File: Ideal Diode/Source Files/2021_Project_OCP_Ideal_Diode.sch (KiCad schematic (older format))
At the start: 21 parts, among them P101 SMD_1POS_8MM, P102 SMD_1POS_8MM, P103 SMD_1POS_8MM, P104 SMD_1POS_8MM, P105 MH_1POS_2.5MM, P106 MH_1POS_2.5MM, P107 MH_1POS_2.5MM, P108 MH_1POS_2.5MM, Q101 PSMNR70-40SSHJ, U101 ZXTR2112F-7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

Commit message: Add files via upload
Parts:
- removed R101: RC0603FR-07100RL, Passives:R_0603_Handsolder, symbol Resistors_0603:RC0603FR-07100RL
- removed R104: ERA-3AEB103V, Passives:R_0603_Handsolder, symbol Resistors_0603:ERA-3AEB103V
- removed R105: RMCF0603ZT0R00, Passives:R_0603_Handsolder, symbol Resistors_0603:RMCF0603ZT0R00
- added R101: RC0603FR-0716RL, Passives:R_0603_Handsolder, symbol Resistors_0603:RC0603FR-0716RL
- added R104, R105: RC0603FR-07470RL, Passives:R_0603_Handsolder, symbol Resistors_0603:RC0603FR-07470RL
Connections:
- net CATHODE: now also R105.2
- net GND: now also R104.2
- net at U102.1 (OUT): now also R101.1
- net at Q101.1 (G): now also R101.2
- net at U102.3 (IN+): now also R104.1
- net at U102.4 (IN-): now also R105.1
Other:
- note added: "1. REPLACED R104, R105 WITH 16R RESISTOR"
- note added: "20210308_PROJECTS_IdealDiode_A3_00004"
- note added: "A3"
- moved on the sheet: P101, P103
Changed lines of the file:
@@
 Text Notes 8825 825  0    50   ~ 0
 20210120_PROJECTS_IdealDiode_A0_00001
-$Comp
-L Resistors_0603:RC0603FR-07100RL R101
-U 1 1 5FCA2DDC
-P 5825 4950
-F 0 "R101" V 5825 4950 50  0000 C CNN
-F 1 "RC0603FR-07100RL" V 5925 4950 50  0001 C CNN
-F 2 "Passives:R_0603_Handsolder" V 5755 4950 50  0001 C CNN
-F 3 "" V 5905 4950 50  0000 C CNN
-F 4 "Susumu" V 6005 5050 60  0001 C CNN "Manufacturer"
-F 5 "100R" H 5875 5000 50  0000 L CNN "P_Value"
-F 6 "1/10W" V 6125 5250 60  0001 C CNN "P_Rating_U"
-F 7 "1%" H 5900 4875 25  0000 L CNN "P_Tolerance"
-F 8 "0603" H 5900 4925 25  0000 L CNN "Package"
-	1    5825 4950
-	1    0    0    -1
-$EndComp
 Wire Wire Line
 	5825 5100 5825 5150
@@
 Connection ~ 6375 5350
 Wire Wire Line
-	4800 2375 5775 2375
+	4800 2925 5775 2925
 Wire Wire Line
 	4775 5350 5350 5350
@@
 L power:VBUS #PWR0106
 U 1 1 5FCBCFE3
-P 5775 2325
-F 0 "#PWR0106" H 5775 2175 50  0001 C CNN
-F 1 "VBUS" H 5775 2475 50  0000 C CNN
-F 2 "" H 5775 2325 50  0001 C CNN
-F 3 "" H 5775 2325 50  0001 C CNN
-	1    5775 2325
-	1    0    0    -1
-$EndComp
-Wire Wire Line
-	5775 2325 5775 2375
-Connection ~ 5775 2375
-Wire Wire Line
-	5775 2375 6425 2375
+P 5775 2875
+F 0 "#PWR0106" H 5775 2725 50  0001 C CNN
+F 1 "VBUS" H 5775 3025 50  0000 C CNN
+F 2 "" H 5775 2875 50  0001 C CNN
+F 3 "" H 5775 2875 50  0001 C CNN
+	1    5775 2875
+	1    0    0    -1
+$EndComp
+Wire Wire Line
+	5775 2875 5775 2925
+Connection ~ 5775 2925
+Wire Wire Line
+	5775 2925 6425 2925
 $Comp
 L power:GND #PWR0110
@@
 Text Notes 7150 1300 0    47   ~ 0
 1. ADDED DESD34VS2SO (D101)\n2. ADDED 10K (R104)\n3. REPLACED Q101 WITH PSMNR70-40SSHJ\n4. ADDED R105 0R\n5. ADDED R106 ThermaLink
-$Comp
-L Resistors_0603:ERA-3AEB103V R104
-U 1 1 601B6BEA
-P 6375 4400
-F 0 "R104" V 6375 4400 50  0000 C CNN
-F 1 "ERA-3AEB103V" V 6475 4400 50  0001 C CNN
-F 2 "Passives:R_0603_Handsolder" V 6305 4400 50  0001 C CNN
-F 3 "" V 6455 4400 50  0000 C CNN
-F 4 "Panasonic Electronic Components" V 6555 4500 60  0001 C CNN "Manufacturer"
-F 5 "10k" H 6425 4450 50  0000 L CNN "P_Value"
-F 6 "1/10W" V 6675 4700 60  0001 C CNN "P_Rating_U"
-F 7 "0.1%" H 6500 4325 25  0000 C CNN "P_Tolerance"
-F 8 "0603" H 6450 4375 25  0000 L CNN "Package"
-F 9 "P10KDBCT-ND" H 6375 4400 25  0001 C CNN "P_Digikey"
-	1    6375 4400
-	1    0    0    -1
-$EndComp
 Wire Wire Line
 	6375 4250 6375 4025
@@
 	0    -1   1    0
 $EndComp
-$Comp
-L Resistors_0603:RMCF0603ZT0R00 R105
-U 1 1 601B32BA
-P 5350 4400
-F 0 "R105" V 5350 4400 50  0000 C CNN
-F 1 "RMCF0603ZT0R00" V 5450 4400 50  0001 C CNN
-F 2 "Passives:R_0603_Handsolder" V 5280 4400 50  0001 C CNN
-F 3 "" V 5430 4400 50  0000 C CNN
-F 4 "Stackpole Electronics Inc." V 5530 4500 60  0001 C CNN "Manufacturer"
-F 5 "0R" H 5400 4450 50  0000 L CNN "P_Value"
-F 6 "1/10W" V 5650 4700 50  0001 C CNN "P_Rating"
-F 7 "0603" H 5425 4375 25  0000 L CNN "Package"
-	1    5350 4400
-	1    0    0    -1
-$EndComp
 Wire Wire Line
 	5350 4250 5350 4025
@@
 L Connectors:SMD_1POS_8MM P103
 U 1 1 601CC9B9
-P 6575 2375
-F 0 "P103" H 6375 2375 60  0000 C CNN
-F 1 "SMD_1POS_8MM" H 6525 1975 50  0001 C CNN
-F 2 "Connectors_sg:SMD_1POS_8MM" V 7175 2175 60  0001 C CNN
-F 3 "" H 6575 2525 60  0001 C CNN
-F 4 "CUSTOM" H 7125 3025 50  0001 C CNN "Manufacturer"
-F 5 "1POS" H 6633 2508 50  0001 C CNN "P_Value"
-F 6 "##" H 7125 2825 60  0001 C CNN "P_Rating_U"
-F 7 "8MM" H 7125 2925 60  0001 C CNN "P_Tolerance"
-F 8 "SMD" H 7125 3125 60  0001 C CNN "Package"
-	1    6575 2375
+P 6575 2925
+F 0 "P103" H 6375 2925 60  0000 C CNN
+F 1 "SMD_1POS_8MM" H 6525 2525 50  0001 C CNN
+F 2 "Connectors_sg:SMD_1POS_8MM" V 7175 2725 60  0001 C CNN
+F 3 "" H 6575 3075 60  0001 C CNN
+F 4 "CUSTOM" H 7125 3575 50  0001 C CNN "Manufacturer"
+F 5 "1POS" H 6633 3058 50  0001 C CNN "P_Value"
+F 6 "##" H 7125 3375 60  0001 C CNN "P_Rating_U"
+F 7 "8MM" H 7125 3475 60  0001 C CNN "P_Tolerance"
+F 8 "SMD" H 7125 3675 60  0001 C CNN "Package"
+	1    6575 2925
 	-1   0    0    1
 $EndComp
@@
 L Connectors:SMD_1POS_8MM P101
 U 1 1 601CD7CA
-P 4650 2375
-F 0 "P101" H 4450 2375 60  0000 C CNN
-F 1 "SMD_1POS_8MM" H 4600 1975 50  0001 C CNN
-F 2 "Connectors_sg:SMD_1POS_8MM" V 5250 2175 60  0001 C CNN
-F 3 "" H 4650 2525 60  0001 C CNN
-F 4 "CUSTOM" H 5200 3025 50  0001 C CNN "Manufacturer"
-F 5 "1POS" H 4708 2508 50  0001 C CNN "P_Value"
-F 6 "##" H 5200 2825 60  0001 C CNN "P_Rating_U"
-F 7 "8MM" H 5200 2925 60  0001 C CNN "P_Tolerance"
-F 8 "SMD" H 5200 3125 60  0001 C CNN "Package"
-	1    4650 2375
+P 4650 2925
+F 0 "P101" H 4450 2925 60  0000 C CNN
+F 1 "SMD_1POS_8MM" H 4600 2525 50  0001 C CNN
+F 2 "Connectors_sg:SMD_1POS_8MM" V 5250 2725 60  0001 C CNN
+F 3 "" H 4650 3075 60  0001 C CNN
+F 4 "CUSTOM" H 5200 3575 50  0001 C CNN "Manufacturer"
+F 5 "1POS" H 4708 3058 50  0001 C CNN "P_Value"
+F 6 "##" H 5200 3375 60  0001 C CNN "P_Rating_U"
+F 7 "8MM" H 5200 3475 60  0001 C CNN "P_Tolerance"
+F 8 "SMD" H 5200 3675 60  0001 C CNN "Package"
+	1    4650 2925
 	1    0    0    -1
 $EndComp
@@
 Wire Notes Line style solid
 	8800 500  8800 1375
+Text Notes 4825 1500 0    50   ~ 0
+2021/02/04
+Text Notes 5375 1500 0    50   ~ 0
+A3
+Wire Notes Line style solid
+	4800 1375 4800 1650
+Wire Notes Line style solid
+	4800 1650 10500 1650
+Wire Notes Line style solid
+	10500 1650 10500 1375
+Wire Notes Line style solid
+	8800 1375 8800 1650
+Wire Notes Line style solid
+	7125 1375 7125 1650
+Wire Notes Line style solid
+	6125 1375 6125 1650
+Wire Notes Line style solid
+	5350 1375 5350 1650
+Text Notes 6150 1500 0    50   ~ 0
+STEVEN GUZMAN
+Text Notes 7150 1500 0    39   ~ 0
+1. REPLACED R104, R105 WITH 16R RESISTOR
+$Comp
+L Resistors_0603:RC0603FR-07470RL R104
+U 1 1 60507F7B
+P 6375 4400
+F 0 "R104" V 6375 4300 50  0000 L CNN
+F 1 "RC0603FR-07470RL" H 6675 5025 50  0001 C CNN
+F 2 "Passives:R_0603_Handsolder" H 6925 4925 50  0001 C CNN
+F 3 "" V 6455 4400 50  0000 C CNN
+F 4 "Yageo" V 6555 4500 60  0001 C CNN "Manufacturer"
+F 5 "470R" H 6425 4450 50  0000 L CNN "P_Value"
+F 6 "1/10W" V 6675 4700 60  0001 C CNN "P_Rating_U"
+F 7 "1%" H 6450 4325 25  0000 L CNN "P_Tolerance"
+F 8 "0603" H 6450 4375 25  0000 L CNN "Package"
+F 9 "311-470HRCT-ND " H 6525 5100 50  0001 C CNN "P_Digikey"
+	1    6375 4400
+	1    0    0    -1
+$EndComp
+$Comp
+L Resistors_0603:RC0603FR-07470RL R105
+U 1 1 60509232
+P 5350 4400
+F 0 "R105" V 5350 4300 50  0000 L CNN
+F 1 "RC0603FR-07470RL" H 5650 5025 50  0001 C CNN
+F 2 "Passives:R_0603_Handsolder" H 5900 4925 50  0001 C CNN
+F 3 "" V 5430 4400 50  0000 C CNN
+F 4 "Yageo" V 5530 4500 60  0001 C CNN "Manufacturer"
+F 5 "470R" H 5400 4450 50  0000 L CNN "P_Value"
+F 6 "1/10W" V 5650 4700 60  0001 C CNN "P_Rating_U"
+F 7 "1%" H 5425 4325 25  0000 L CNN "P_Tolerance"
+F 8 "0603" H 5425 4375 25  0000 L CNN "Package"
+F 9 "311-470HRCT-ND " H 5500 5100 50  0001 C CNN "P_Digikey"
+	1    5350 4400
+	-1   0    0    -1
+$EndComp
+$Comp
+L Resistors_0603:RC0603FR-0716RL R101
+U 1 1 6050A967
+P 5825 4950
+F 0 "R101" V 5825 4850 50  0000 L CNN
+F 1 "RC0603FR-0716RL" V 5925 4950 50  0001 C CNN
+F 2 "Passives:R_0603_Handsolder" V 5755 4950 50  0001 C CNN
+F 3 "" V 5905 4950 50  0000 C CNN
+F 4 "Yageo" V 6005 5050 60  0001 C CNN "Manufacturer"
+F 5 "16R" H 5875 5000 50  0000 L CNN "P_Value"
+F 6 "1/10W" V 6125 5250 60  0001 C CNN "P_Rating_U"
+F 7 "1%" H 5900 4875 25  0000 L CNN "P_Tolerance"
+F 8 "0603" H 5900 4925 25  0000 L CNN "Package"
+	1    5825 4950
+	1    0    0    -1
+$EndComp
+Text Notes 8825 1500 0    50   ~ 0
+20210308_PROJECTS_IdealDiode_A3_00004
 $EndSCHEMATC

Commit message: Add files via upload
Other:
- note added: "1. REPLACED R104, R105 WITH 470R RESISTOR\n2. REPLACED R101 WITH 16R RESISTOR"
- note removed: "1. REPLACED R104, R105 WITH 16R RESISTOR"
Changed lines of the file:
@@
 Text Notes 6150 1500 0    50   ~ 0
 STEVEN GUZMAN
-Text Notes 7150 1500 0    39   ~ 0
-1. REPLACED R104, R105 WITH 16R RESISTOR
+Text Notes 7150 1550 0    39   ~ 0
+1. REPLACED R104, R105 WITH 470R RESISTOR\n2. REPLACED R101 WITH 16R RESISTOR
 $Comp
 L Resistors_0603:RC0603FR-07470RL R104

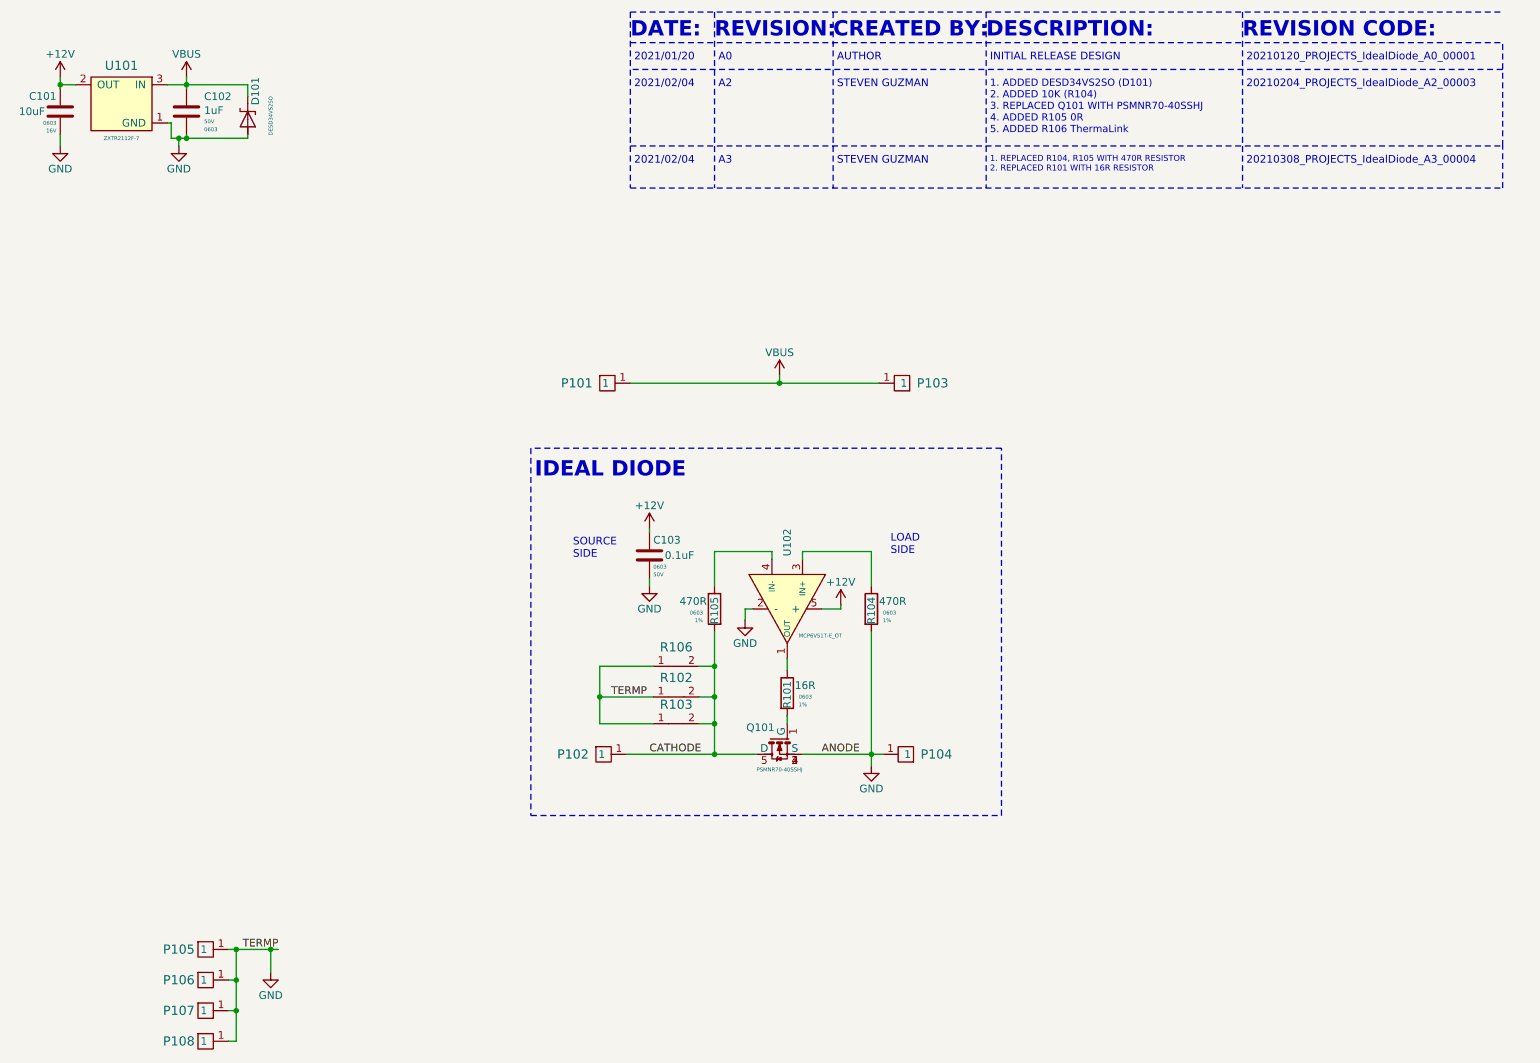
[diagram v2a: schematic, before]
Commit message: Version A4
Updated to Version A4 of ideal diode
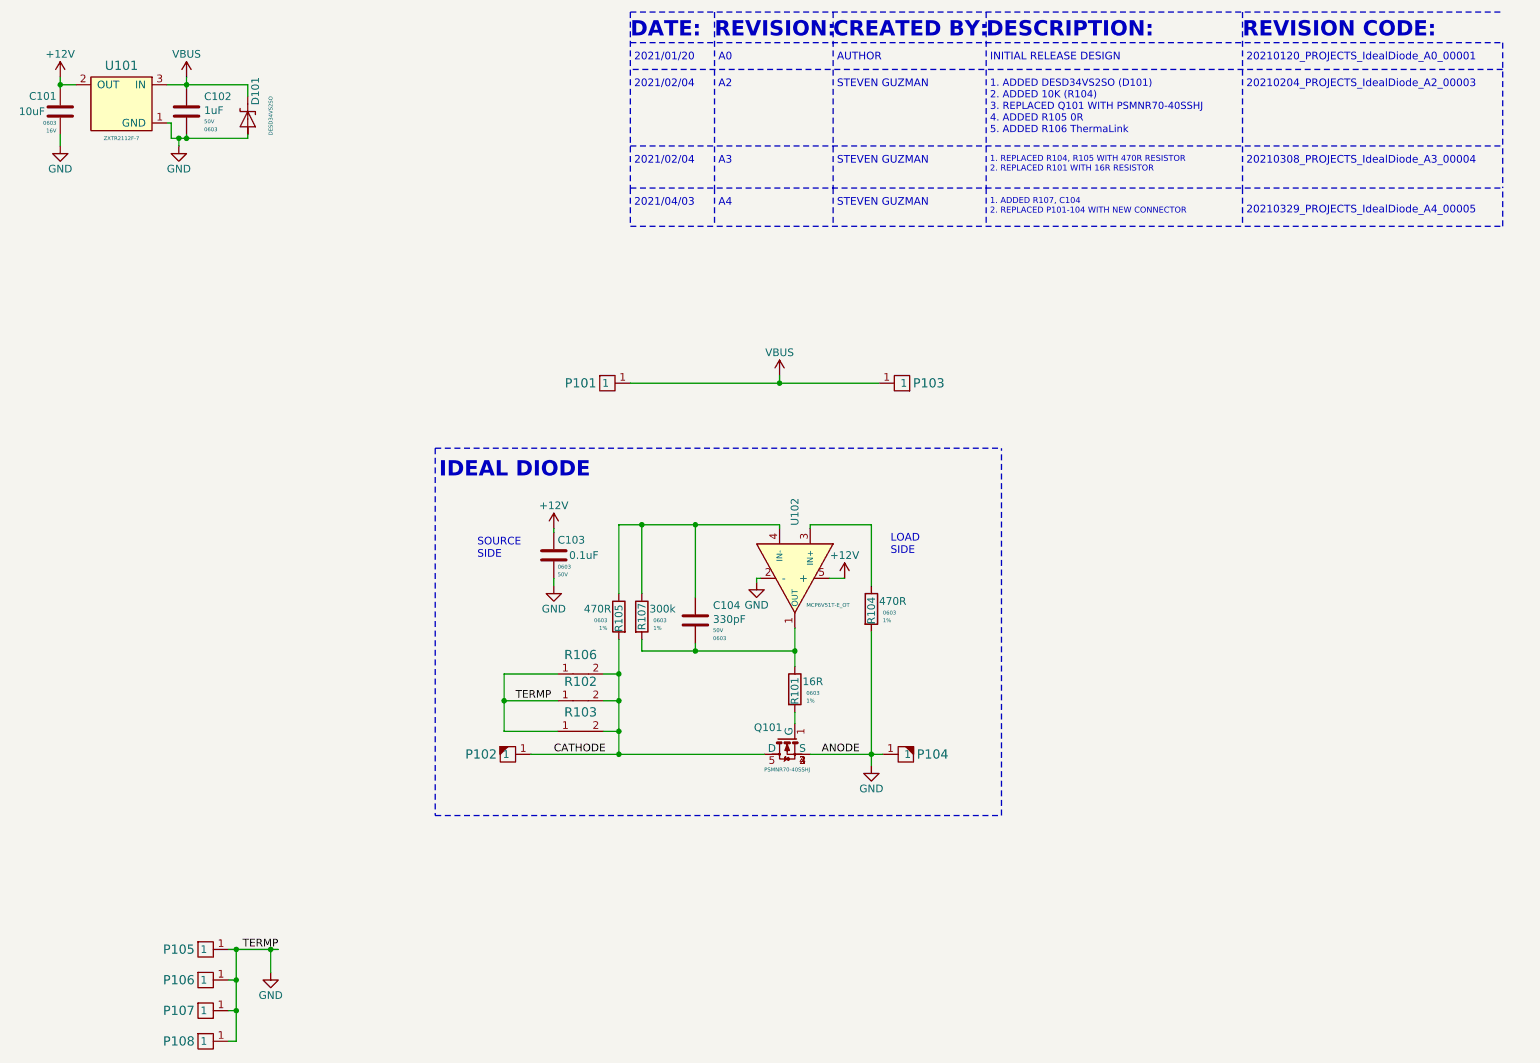
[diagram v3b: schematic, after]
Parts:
- removed P101, P102, P103, P104: SMD_1POS_8MM, Connectors_sg:SMD_1POS_8MM, symbol Connectors:SMD_1POS_8MM
- added C104: C0603C331J5GACTU, Passives:C_0603_Handsolder, symbol Capacitor_0603:C0603C331J5GACTU
- added P101, P103: 2.5x2.5mm_pad, Terminal Blocks:pad_2.5x2.5mm, symbol Terminal_Blocks:2.5x2.5mm_pad
- added P102, P104: 7460305, Terminal Blocks:7460305_HASL, symbol Connectors:7460305
- added R107: RMCF0603FT300K, Passives:R_0603_Handsolder, symbol Resistors_0603:RMCF0603FT300K
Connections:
- net CATHODE: now also P102.1
- net GND: now also P104.1
- net VBUS: now also P101.1, P103.1
- net at R101.1, U102.1 (OUT): now also C104.2, R107.2
- net at R105.1, U102.4 (IN-): now also C104.1, R107.1
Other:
- note added: "1. ADDED R107, C104\n2. REPLACED P101-104 WITH NEW CONNECTOR"
- note added: "2021/04/03"
- note added: "20210329_PROJECTS_IdealDiode_A4_00005"
- note added: "A4"
- moved on the sheet: C103, Q101, R101, R102, R103, R105, R106, U102
